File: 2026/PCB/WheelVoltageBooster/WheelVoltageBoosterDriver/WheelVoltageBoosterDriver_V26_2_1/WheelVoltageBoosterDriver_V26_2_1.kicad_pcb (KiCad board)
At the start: 2 copper layers, 100 x 65 mm, 190 parts, among them J1 Conn_01x04_Socket, J10 Conn_01x03_Socket, J11 Conn_01x05_Socket, J13 Conn_01x04_Socket, J2 Conn_01x02_Pin, J3 Conn_01x04_Socket, J4 Conn_01x04_Socket, J5 Conn_01x04_Socket, J6 Conn_01x02_Pin, J7 Conn_01x02_Pin, J8 Conn_01x07_Socket, J9 Conn_01x03_Socket, SW1 SW_MEC_5E, SW2 SW_MEC_5E, U1 MAX3051, U10 HIP2101EIBZT, U2 TMP235AQDCKRQ1, U3 STM32H523CEU6, U4 TMP235AQDCKRQ1, U5 MAX20405AFOA/VY+, U6 MCP1703AT-3302E/CB, U7 MAX20405AFOA/VY+, U8 MAX15158A, U9 HIP2101EIBZT, Y1 CSTNE16M0V530000R0

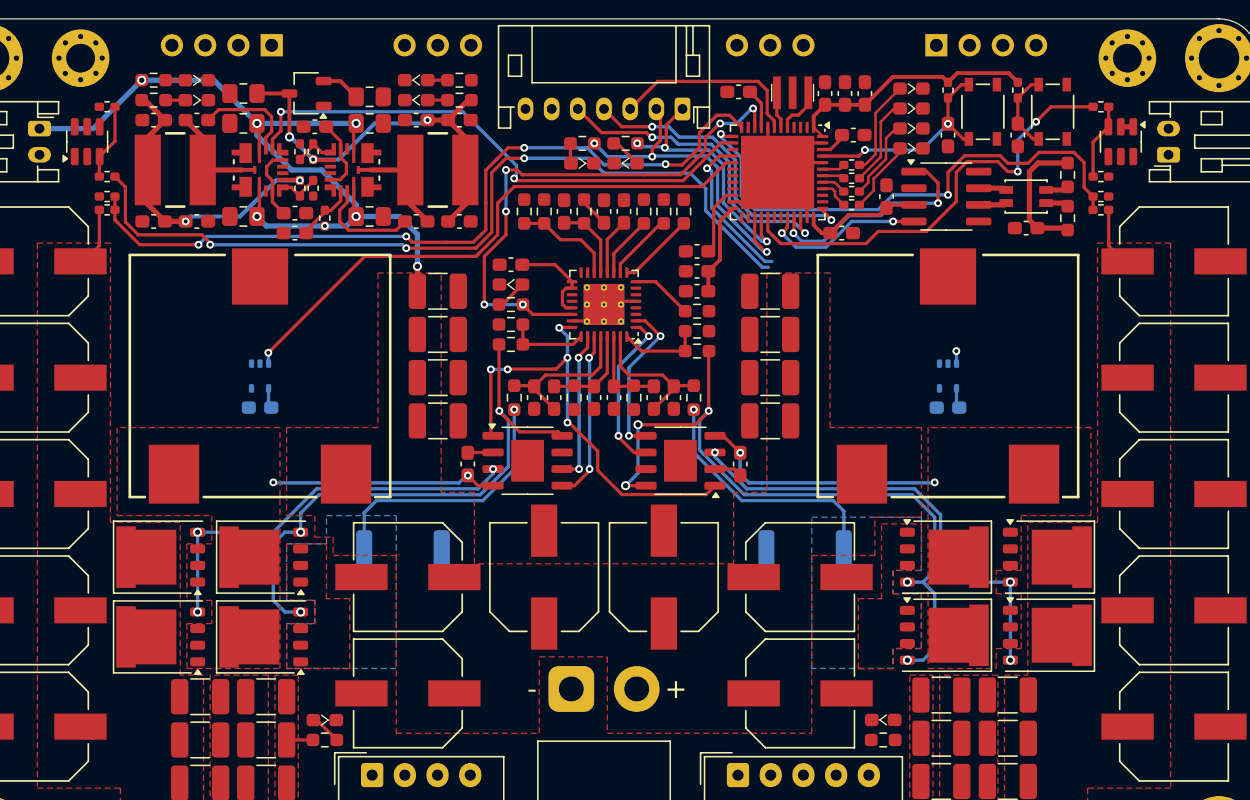
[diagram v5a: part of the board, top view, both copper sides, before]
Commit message: BIAS系統の配線完了
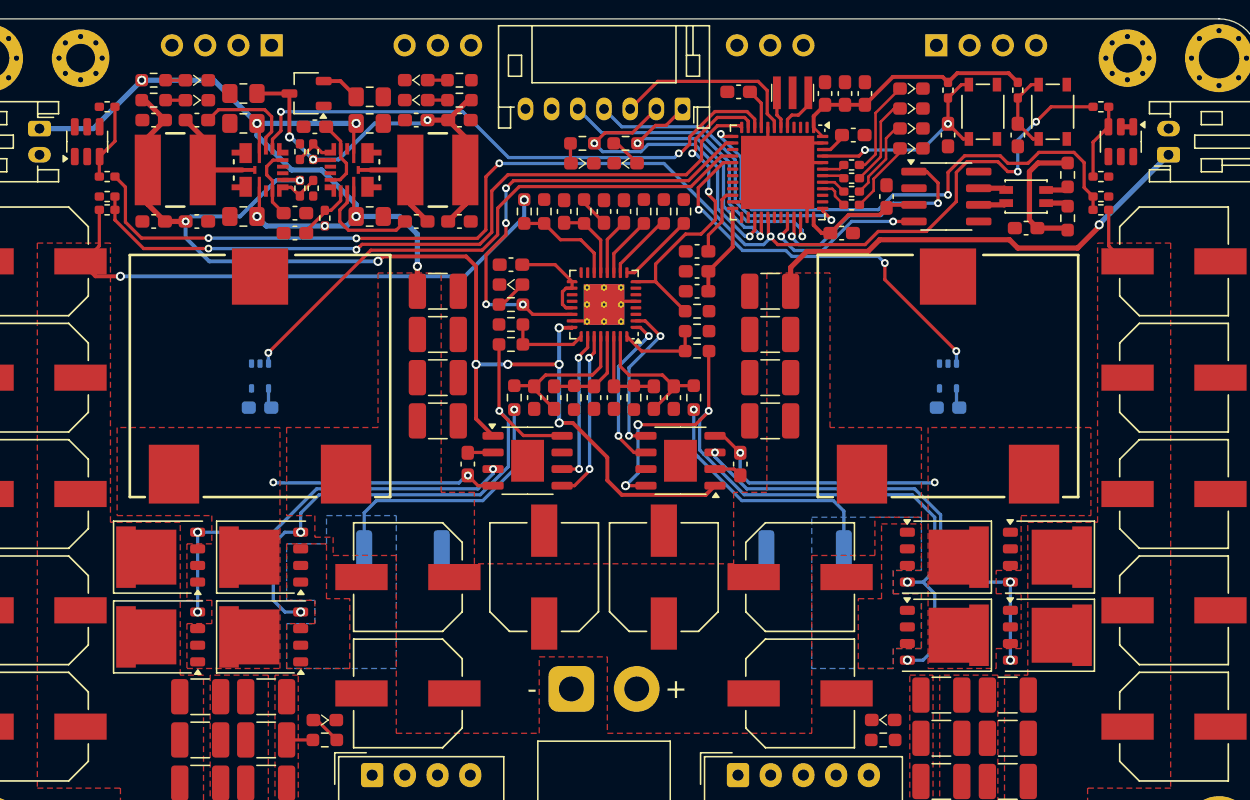
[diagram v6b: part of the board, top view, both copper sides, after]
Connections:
- U3 pad 10: /Power_Circuit/MREN -> /Power_Circuit/10VEN
- U3 pad 14: /Power_Circuit/10VEN -> /Power_Circuit/MREN
- U3 pad 16: TEMP1 -> TEMP2
- U3 pad 17: TEMP2 -> TEMP1
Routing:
- net 50V: track 11.4 -> 48.4 mm, vias 0 -> 2
- net 25V: track 65.9 -> 99.7 mm, vias 7 -> 8
- net 10V: track 58.8 -> 89.6 mm, vias 7 -> 8
- net /Power_Circuit/PGOOD: track 4.70 -> 24.5 mm, vias 0 -> 2
- net TEMP1: track 12.9 -> 31.0 mm, vias 2 -> 3
- net GND: track 24.3 -> 12.2 mm
- net /Power_Circuit/MREN: track 41.2 -> 35.2 mm, vias 6 -> 4
- net 6V5: track 32.5 -> 29.6 mm
- net /Power_Circuit/MRVFB1: track 59.8 -> 57.3 mm, vias 4 -> 2
- net Net-(U7-LX): track 7.38 -> 4.88 mm
- net FET_FAN: track 97.8 -> 95.5 mm, vias 5 -> 6
- net /Power_Circuit/10VEN: track 41.8 -> 43.4 mm
- net Net-(U3-PH0-OSC_IN): track 3.61 -> 2.65 mm
- net 3V3: track 45.1 -> 44.2 mm
- net USART1_TX: track 25.5 -> 24.6 mm, vias 3 -> 2
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
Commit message: DRC通過
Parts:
- moved C2 3.94 mm to (123.7, 96.1)
- moved C24 3.94 mm to (176.3, 96.1)
- moved U2 3.94 mm to (123.7, 93.7)
- moved U4 3.94 mm to (176.3, 93.7)
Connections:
- L1 pad 3: (no net) -> GND
- L2 pad 3: (no net) -> GND
- U10 pad 9: (no net) -> GND
- U9 pad 9: (no net) -> GND
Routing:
- net 3V3: track 44.2 -> 161.4 mm, vias 0 -> 9
- net 6V5: track 29.6 -> 131.7 mm, vias 3 -> 5
- net CANH: track 1.41 -> 94.9 mm, vias 0 -> 2
- net CANL: track 1.41 -> 90.1 mm, vias 0 -> 1
- net nRST: track 20.7 -> 41.9 mm, vias 0 -> 2
- net Net-(U8-BIAS): track 7.50 -> 24.9 mm, vias 0 -> 2
- net 25V: track 99.7 -> 115.5 mm
- net Net-(J7-Pin_2): track 0.00 -> 8.23 mm
- net Net-(J2-Pin_2): track 0.95 -> 8.04 mm
- net TEMP1: track 31.0 -> 35.1 mm
- net TEMP2: track 43.7 -> 47.7 mm
- net Net-(D1-A): track 0.00 -> 2.16 mm
- net 50V: track 48.4 -> 50.3 mm
- net CAN1_TX: track 18.2 -> 17.4 mm
- net /Power_Circuit/10VEN: track 43.4 -> 44.3 mm
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- added copper zone on B.Cu, net 25V
- added copper zone on B.Cu, net 3V3
- added copper zone on F.Cu, net 3V3
- added copper zone on B.Cu, net 50V
- added copper zone on B.Cu, net GND

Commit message: 設計完了
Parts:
- added REF**: Symbol_HighVoltage_Triangle_6x6mm_Copper, Symbol:Symbol_HighVoltage_Triangle_6x6mm_Copper, B.Cu at (125.7, 74.3)
- U8: footprint Package_DFN_QFN:TQFN-32-1EP_5x5mm_P0.5mm_EP3.1x3.1mm_ThermalVias -> Package_DFN_QFN:TQFN-32-1EP_5x5mm_P0.5mm_EP3.1x3.1mm
- moved J1 7.62 mm to (175.4, 125.5), turned to -90 degrees
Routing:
- net /Power_Circuit/PGOOD: track 24.5 -> 26.8 mm
- net 25V: track 115.5 -> 116.4 mm
- net GND: vias 170 -> 195
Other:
- board text added: "BLACK FANG 465 V26.2.1"
- board text added: "Wheel Voltage Booster Rot_No.16OCT2025-26-2-1 Git_No.5526689080ee60dcab9b672148484d09ca6e76fc"
- board text removed: "BLACK FANG 465 V26.1.1"
- board text removed: "Wheel Voltage Booster Rot_No.02JUL2025-26-1-1 Git_No.5526689080ee60dcab9b672148484d09ca6e76fc"
